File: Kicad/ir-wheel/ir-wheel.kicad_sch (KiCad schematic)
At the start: 8 parts, among them IC1 TTE-OPB606, IC2 TTE-OPB606, K1 MOLEX-MICRO-LATCH-03-RIGHT-AN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, K2 MOLEX-MICRO-LATCH-03-RIGHT-AN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

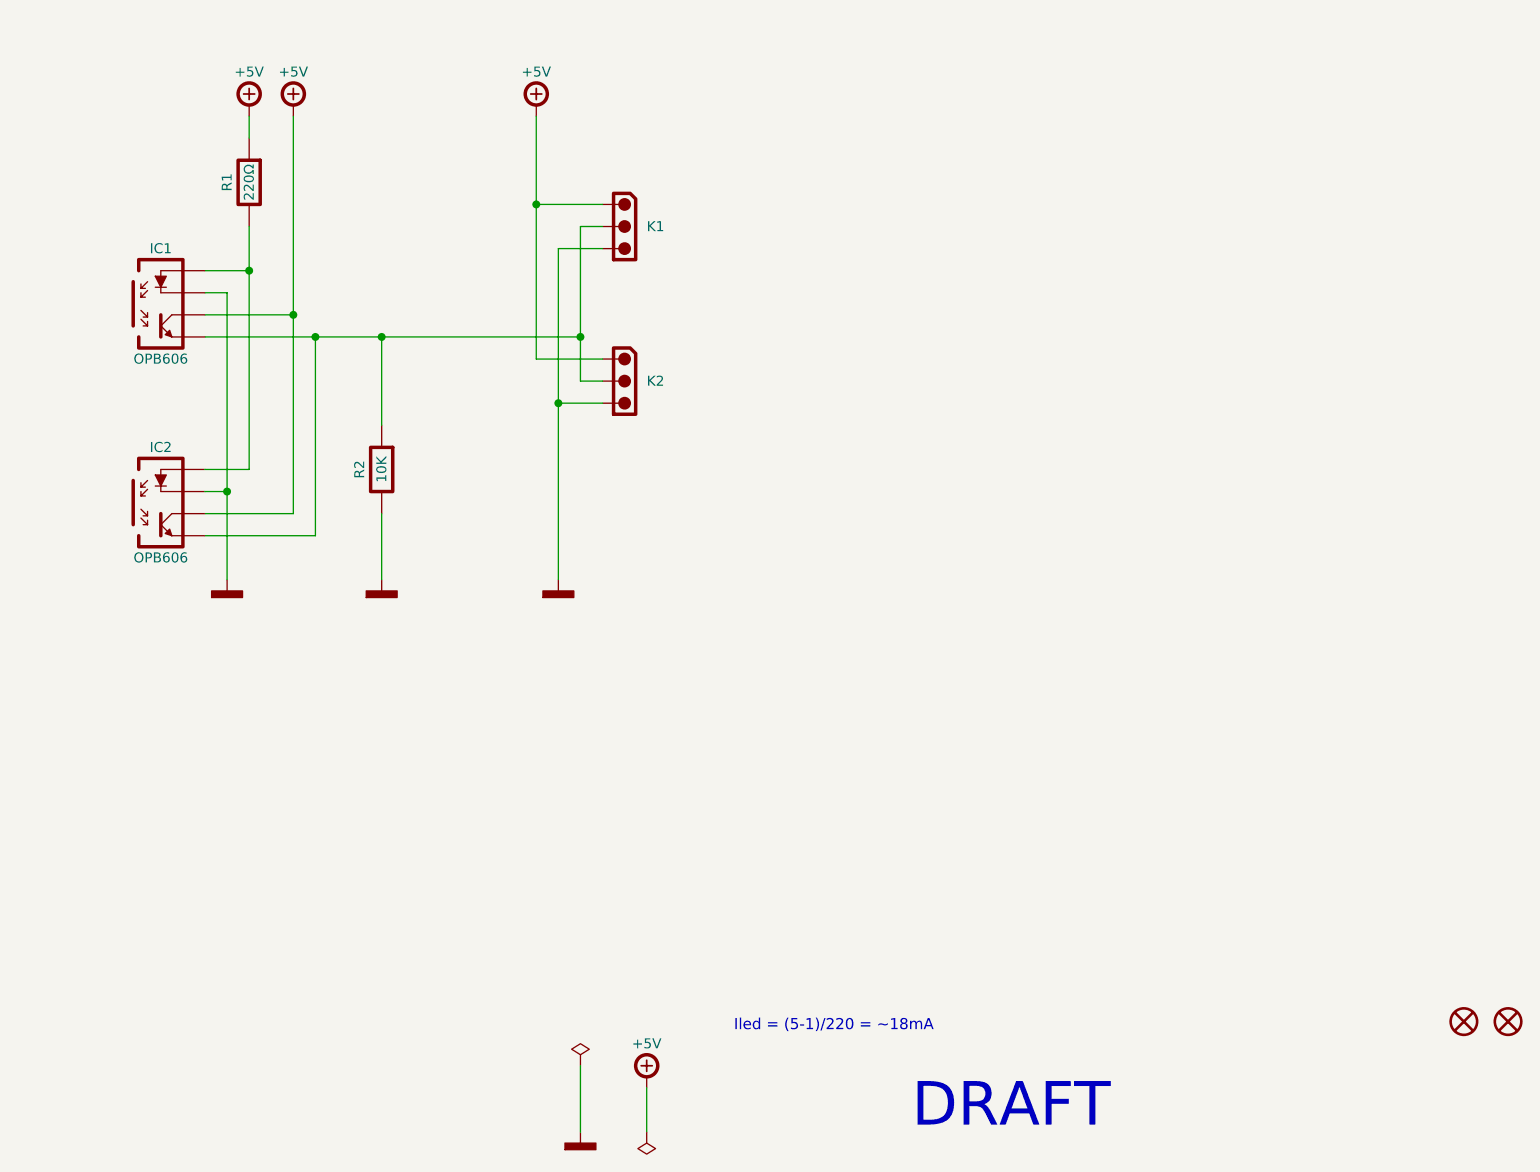
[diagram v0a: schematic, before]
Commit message: Add IR Wheel
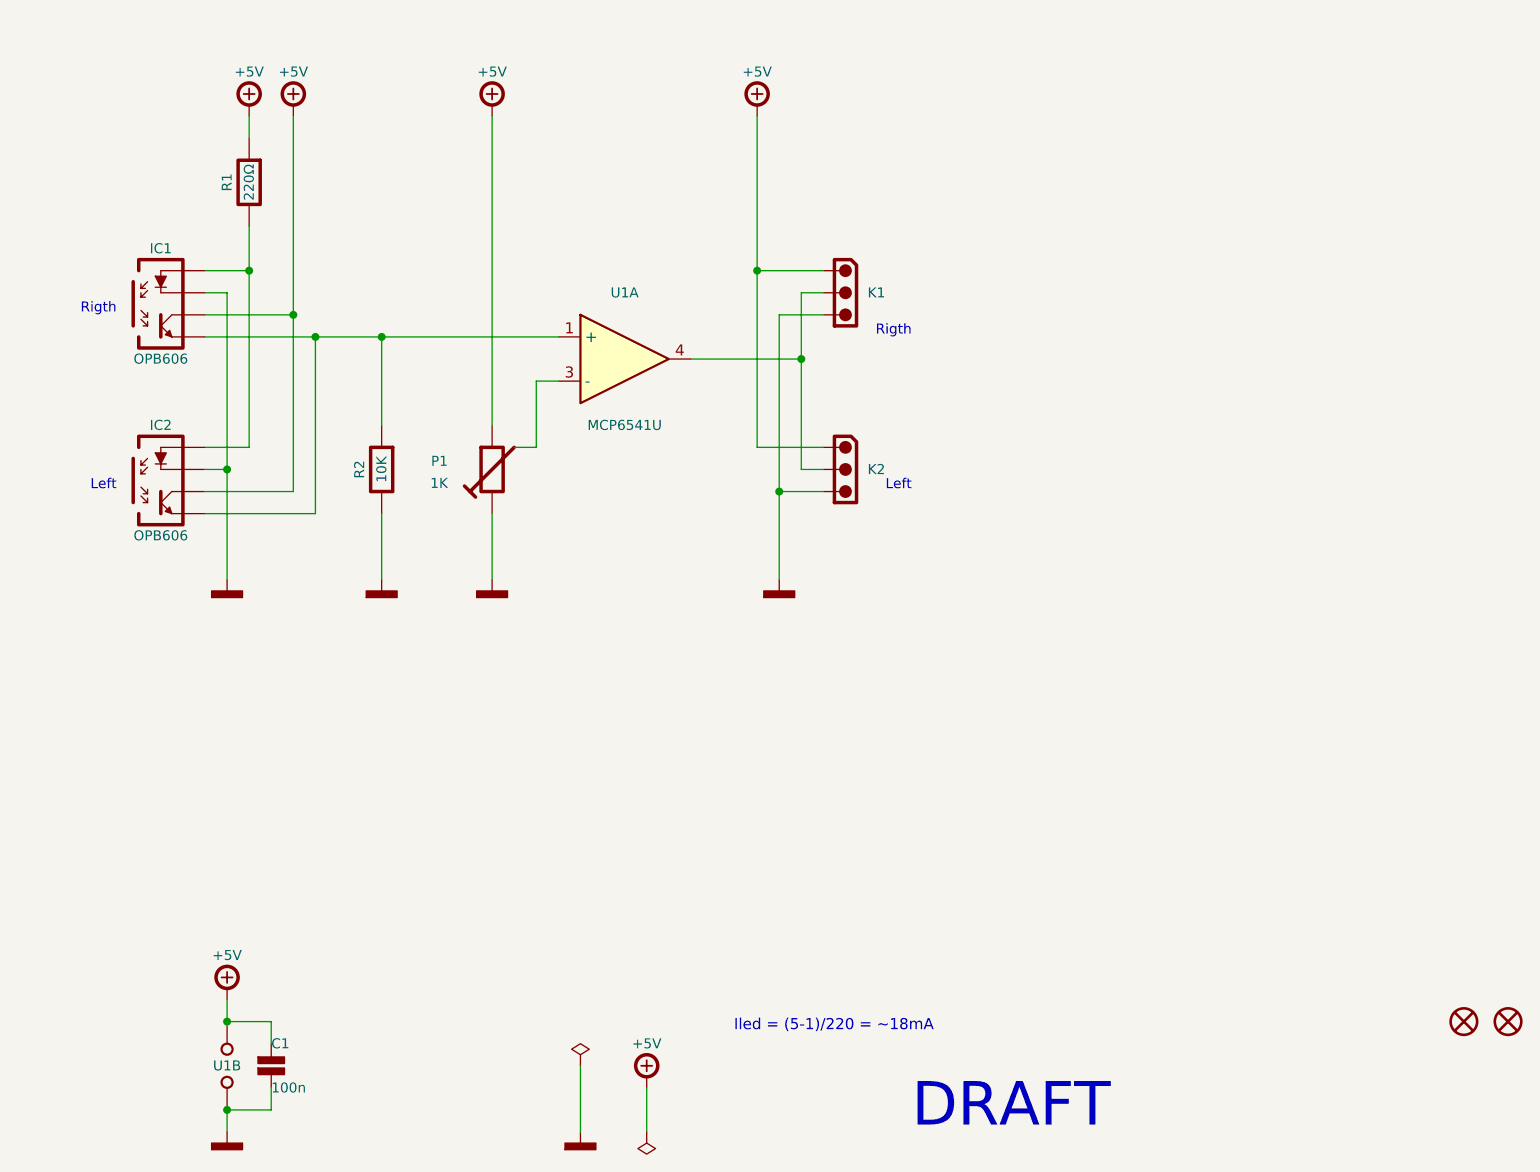
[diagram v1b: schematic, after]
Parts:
- added C1: 100n, tronixio:CAPACITOR-1206, symbol tronixio:C-1206
- added P1: BOURNS-TC33X-1K, tronixio:zzzTC33X, symbol tronixio:BOURNS-TC33X-1K
- added U1: MICROCHIP-MCP6541-SOT-23, tronixio:SOT-23-5, symbol tronixio:MICROCHIP-MCP6541-SOT-23
- IC1, IC2: footprint tronixio:zzzOPB-606 -> tronixio:zzOPB-606
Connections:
- net +5V: now also C1.1, P1.1, U1.5 (VDD)
- net GND: now also C1.2, P1.3, U1.2 (GND)
- net at IC1.4 (EMITTER), IC2.4 (EMITTER), R2.2: now also U1.1 (+); no longer K1.2, K2.2
- new net: P1.2, U1.3 (-)
- new net: K1.2, K2.2, U1.4
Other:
- note added: "Left"
- note added: "Rigth"
- moved on the sheet: IC2, K1, K2

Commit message: Update IR WHEEL
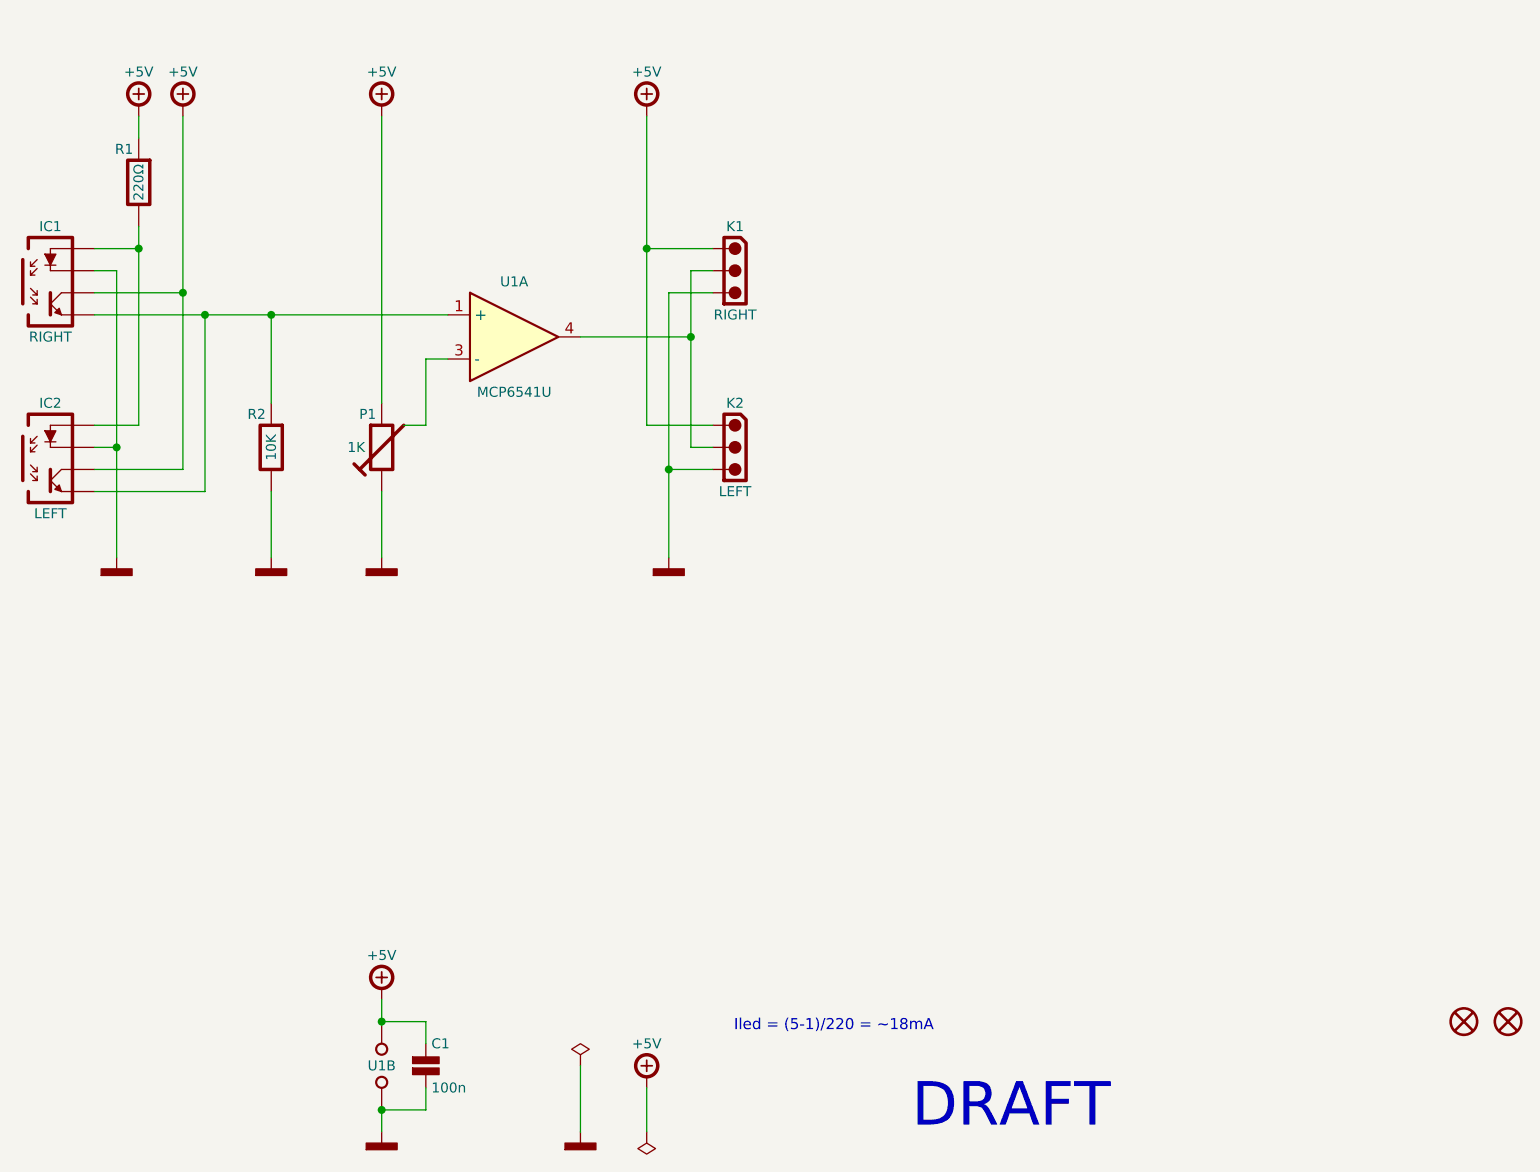
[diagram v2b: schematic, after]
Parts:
- IC1: Name OPB606 -> RIGHT
- IC2: Name OPB606 -> LEFT
- K1: value MOLEX-MICRO-LATCH-03-RIGHT-ANGLE -> RIGHT
- K2: value MOLEX-MICRO-LATCH-03-RIGHT-ANGLE -> LEFT
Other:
- note removed: "Left"
- note removed: "Rigth"
- moved on the sheet: C1, IC1, IC2, K1, K2, P1, R1, R2, U1A, U1B

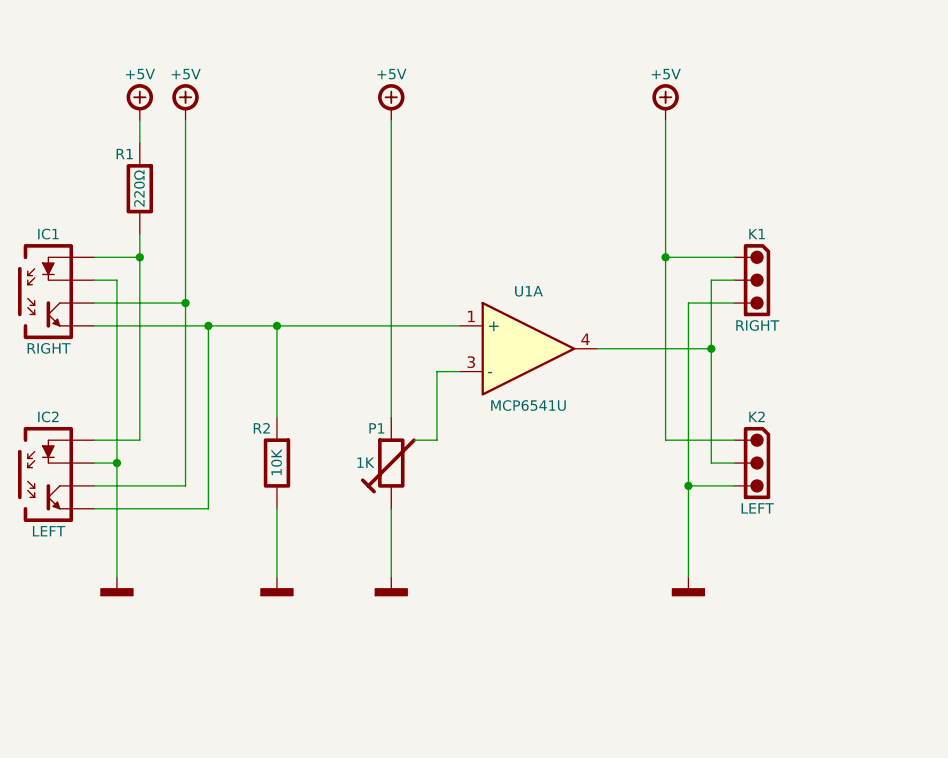
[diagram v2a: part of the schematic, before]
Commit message: Update IR WHEEL
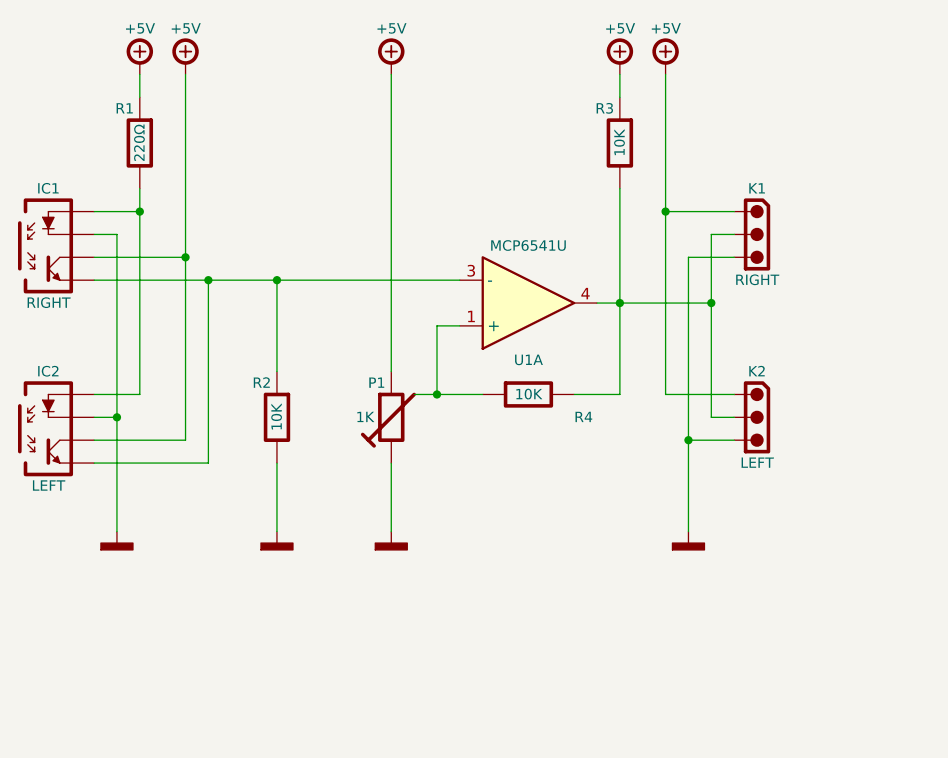
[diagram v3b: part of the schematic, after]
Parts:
- added R3, R4: 10K, tronixio:RESISTOR-1206, symbol tronixio:R-1206
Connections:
- net +5V: now also R3.2
- net at IC1.4 (EMITTER), IC2.4 (EMITTER), R2.2: now also U1.3 (-); no longer U1.1 (+)
- net at P1.2: now also U1.1 (+), R4.2; no longer U1.3 (-)
- net at K1.2, K2.2, U1.4: now also R3.1, R4.1
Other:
- moved on the sheet: IC1, IC2, K1, K2, P1, R1, R2, U1A

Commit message: Update
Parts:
- added C2: 1µ, tronixio:CAPACITOR-1206, symbol tronixio:C-1206
- K1, K2: Mouser (none) -> 538-53254-0370
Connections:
- net +5V: now also C2.1
- net GND: now also C2.2
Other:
- moved on the sheet: C1, U1B

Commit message: Update
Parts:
- removed P1: BOURNS-TC33X-1K, tronixio:zzzTC33X, symbol tronixio:BOURNS-TC33X-1K
- removed R4: 10K, tronixio:RESISTOR-1206, symbol tronixio:R-1206
- added P1: BOURNS-TC33X-200K, tronixio:zzzTC33X, symbol tronixio:BOURNS-TC33X-200K
- R2: value 10K -> 100K
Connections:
- net +5V: now also P1.1
- net GND: now also P1.3
- net at U1.1 (+): now also P1.2
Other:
- note added: "*"
- note added: "* For Open-Drain Output Comparator."
- note removed: "Iled = (5-1)/220 = ~18mA"
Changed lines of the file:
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@@
     (rev "A")
   )
-  (junction (at 154.94 104.14) (diameter 0) (color 0 0 0 0)
-  )
   (junction (at 144.78 187.96) (diameter 0) (color 0 0 0 0)
   )
@@
   (junction (at 144.78 177.8) (diameter 0) (color 0 0 0 0)
   )
-  (wire (pts (xy 154.94 104.14) (xy 160.02 104.14))
-    (stroke (width 0) (type default) (color 0 0 0 0))
-  )
   (wire (pts (xy 187.96 86.36) (xy 185.42 86.36))
     (stroke (width 0) (type default) (color 0 0 0 0))
@@
   )
   (wire (pts (xy 149.86 111.76) (xy 149.86 119.38))
-    (stroke (width 0) (type default) (color 0 0 0 0))
-  )
-  (wire (pts (xy 170.18 104.14) (xy 175.26 104.14))
     (stroke (width 0) (type default) (color 0 0 0 0))
   )
@@
     (stroke (width 0) (type default) (color 0 0 0 0))
   )
-  (wire (pts (xy 175.26 104.14) (xy 175.26 93.98))
-    (stroke (width 0) (type default) (color 0 0 0 0))
-  )
   (wire (pts (xy 116.84 88.9) (xy 127 88.9))
     (stroke (width 0) (type default) (color 0 0 0 0))
@@
     (stroke (width 0) (type default) (color 0 0 0 0))
   )
-  (text "Iled = (5-1)/220 = ~18mA" (at 208.28 179.07 180)
+  (text "*" (at 172.085 73.66 180)
+    (effects (font (size 1.27 1.27)) (justify right bottom))
+  )
+  (text "* For Open-Drain Output Comparator." (at 218.44 179.07 180)
     (effects (font (size 1.27 1.27)) (justify right bottom))
   )
@@
     (pin "1")
   )
-  (symbol (lib_id "tronixio:R-1206") (at 165.1 104.14 270) (unit 1)
-    (in_bom yes) (on_board yes)
-    (property "Reference" "R4" (id 0) (at 165.1 106.68 90)
-      (effects (font (size 1.15 1.15)))
-    )
-    (property "Value" "10K" (id 1) (at 165.1 104.14 90)
-      (effects (font (size 1.15 1.15)))
-    )
-    (property "Footprint" "tronixio:RESISTOR-1206" (id 2) (at 152.4 104.14 0)
-      (effects (font (size 1 1)) hide)
-    )
-    (property "Datasheet" "" (id 3) (at 165.1 104.14 0)
-      (effects (font (size 1 1)) hide)
-    )
-    (pin "1")
-    (pin "2")
-  )
   (symbol (lib_id "tronixio:POWER-+5V") (at 149.86 68.58 0) (unit 1)
     (in_bom yes) (on_board yes)
@@
     (pin "4")
   )
-  (symbol (lib_id "tronixio:BOURNS-TC33X-1K") (at 149.86 106.68 0) (mirror x) (unit 1)
-    (in_bom yes) (on_board yes)
-    (property "Reference" "P1" (id 0) (at 149.225 102.87 0)
-      (effects (font (size 1.15 1.15)) (justify right))
-    )
-    (property "Value" "BOURNS-TC33X-1K" (id 1) (at 149.86 93.98 0)
-      (effects (font (size 1 1)) hide)
-    )
-    (property "Footprint" "tronixio:zzzTC33X" (id 2) (at 149.86 91.44 0)
-      (effects (font (size 1 1)) hide)
-    )
-    (property "Datasheet" "https://www.bourns.com/pdfs/TC33.pdf" (id 3) (at 149.86 88.9 0)
-      (effects (font (size 1 1)) hide)
-    )
-    (property "Name" "1K" (id 4) (at 147.955 106.68 0)
-      (effects (font (size 1.15 1.15)) (justify right))
-    )
-    (property "Mouser" "652-TC33X-1-102E" (id 5) (at 149.86 86.36 0)
-      (effects (font (size 1 1)) hide)
-    )
-    (pin "1")
-    (pin "2")
-    (pin "3")
-  )
   (symbol (lib_id "tronixio:MOUNTING-HOLE-MASK-3MM") (at 269.24 177.8 0) (unit 1)
     (in_bom yes) (on_board yes)
@@
     )
     (property "Mouser" "538-53254-0370" (id 5) (at 190.5 119.38 0)
+      (effects (font (size 1 1)) hide)
+    )
+    (pin "1")
+    (pin "2")
+    (pin "3")
+  )
+  (symbol (lib_id "tronixio:BOURNS-TC33X-200K") (at 149.86 106.68 0) (mirror x) (unit 1)
+    (in_bom yes) (on_board yes)
+    (property "Reference" "P1" (id 0) (at 149.225 102.235 0)
+      (effects (font (size 1.15 1.15)) (justify right))
+    )
+    (property "Value" "BOURNS-TC33X-200K" (id 1) (at 149.86 93.98 0)
+      (effects (font (size 1 1)) hide)
+    )
+    (property "Footprint" "tronixio:zzzTC33X" (id 2) (at 149.86 91.44 0)
+      (effects (font (size 1 1)) hide)
+    )
+    (property "Datasheet" "https://www.bourns.com/pdfs/TC33.pdf" (id 3) (at 149.86 88.9 0)
+      (effects (font (size 1 1)) hide)
+    )
+    (property "Name" "200K" (id 4) (at 149.225 111.76 0)
+      (effects (font (size 1.15 1.15)) (justify right))
+    )
+    (property "Mouser" "652-TC33X-1-204E" (id 5) (at 149.86 86.36 0)
       (effects (font (size 1 1)) hide)
     )
@@
       (effects (font (size 1.15 1.15)) (justify left))
     )
-    (property "Value" "10K" (id 1) (at 137.16 106.68 90)
+    (property "Value" "100K" (id 1) (at 137.16 106.68 90)
       (effects (font (size 1.15 1.15)))
     )
@@
       (reference "K2") (unit 1) (value "LEFT") (footprint "tronixio:MOLEX-532540370")
     )
-    (path "/4ca7bf5e-0fb5-4f7f-a656-f6abf97882dc"
-      (reference "P1") (unit 1) (value "BOURNS-TC33X-1K") (footprint "tronixio:zzzTC33X")
+    (path "/84dc52bd-ebac-4438-bc22-c0cc58a65008"
+      (reference "P1") (unit 1) (value "BOURNS-TC33X-200K") (footprint "tronixio:zzzTC33X")
     )
     (path "/27578f60-a597-4129-a4e9-161572a644b9"
@@
     )
     (path "/ea32b770-f39c-4bef-9287-4592bd2750e6"
-      (reference "R2") (unit 1) (value "10K") (footprint "tronixio:RESISTOR-1206")
+      (reference "R2") (unit 1) (value "100K") (footprint "tronixio:RESISTOR-1206")
     )
     (path "/a8e56c40-4330-4289-957c-f47bc0dde340"
       (reference "R3") (unit 1) (value "10K") (footprint "tronixio:RESISTOR-1206")
     )
-    (path "/1ee5a4c5-e43a-42a8-8119-838de6e8b38f"
-      (reference "R4") (unit 1) (value "10K") (footprint "tronixio:RESISTOR-1206")
-    )
     (path "/fb5bd579-4dd4-40ae-83f9-527cc0e6dad5"

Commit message: Update
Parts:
- added C3: 1n, tronixio:CAPACITOR-1206, symbol tronixio:C-1206
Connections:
- net GND: now also C3.2
- net at K1.2, K2.2, R3.1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: now also C3.1
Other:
- note added: "* For Open-Drain Output Comparator (eg: MCP6566U)."
- note removed: "* For Open-Drain Output Comparator."
- moved on the sheet: C1, C2, K1, K2, U1B
